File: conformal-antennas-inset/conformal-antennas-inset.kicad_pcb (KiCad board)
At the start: 2 copper layers, 1 part, among them J1 Conn_Coaxial

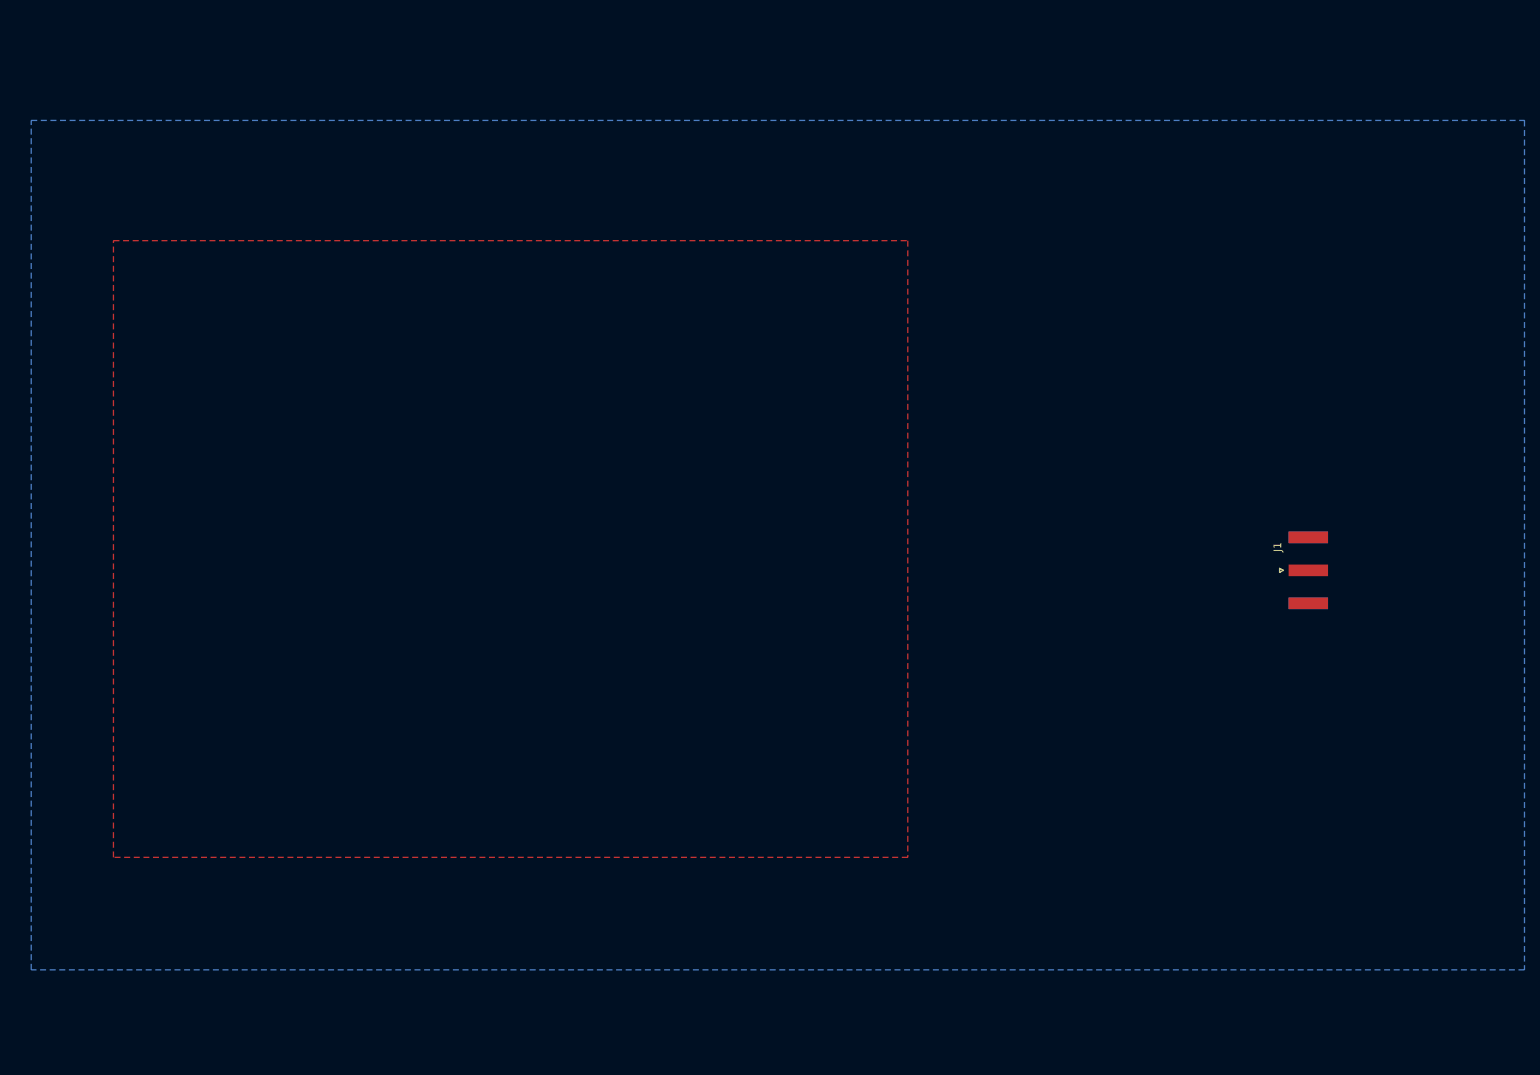
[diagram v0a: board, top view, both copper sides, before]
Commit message: added inset shape
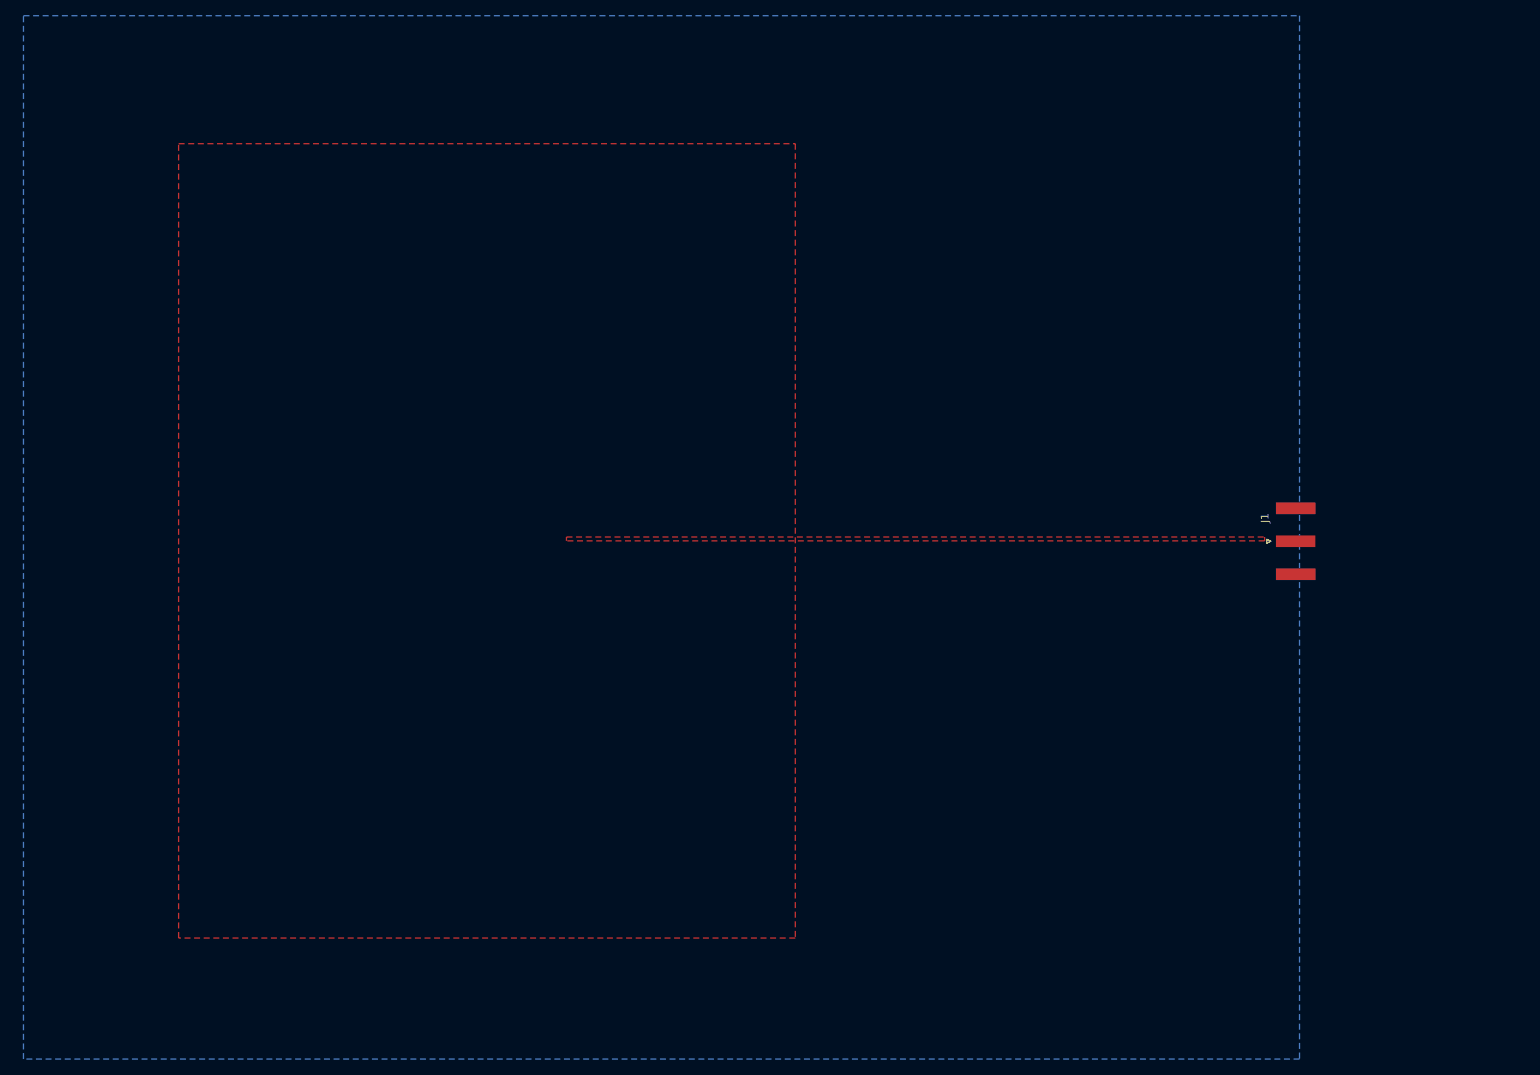
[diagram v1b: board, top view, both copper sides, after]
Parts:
- moved J1 4.09 mm to (213.5, 103.8)
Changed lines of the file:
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@@
 	(footprint "Connector_Coaxial:SMA_Amphenol_132289_EdgeMount"
 		(layer "F.Cu")
-		(at 215.1375 107.5)
+		(at 213.5 103.75)
 		(descr "https://www.amphenolrf.com/library/download/link/link_id/595984/parent/132289/")
 		(tags "SMA")
@@
 		(layer "F.Cu")
 		(hatch edge 0.5)
-		(connect_pads
+		(priority 1)
+		(connect_pads yes
 			(clearance 0.5)
 		)
@@
 		(polygon
 			(pts
-				(xy 61.1 65) (xy 163.5 65) (xy 163.5 144.5) (xy 61.1 144.5)
+				(xy 119.5 103.2) (xy 209.5 103.2) (xy 209.5 103.7) (xy 119.5 103.7)
+			)
+		)
+	)
+	(zone
+		(net 2)
+		(net_name "/Signal")
+		(layer "F.Cu")
+		(hatch edge 0.5)
+		(connect_pads yes
+			(clearance 0.5)
+		)
+		(min_thickness 0.25)
+		(filled_areas_thickness no)
+		(fill yes
+			(thermal_gap 0.5)
+			(thermal_bridge_width 0.5)
+		)
+		(polygon
+			(pts
+				(xy 69.5 52.5) (xy 149 52.5) (xy 149 154.9) (xy 69.5 154.9)
+			)
+		)
+	)
+	(zone
+		(net 0)
+		(net_name "")
+		(layer "F.Cu")
+		(hatch edge 0.1)
+		(connect_pads yes
+			(clearance 0)
+		)
+		(min_thickness 0.25)
+		(filled_areas_thickness no)
+		(keepout
+			(tracks not_allowed)
+			(vias not_allowed)
+			(pads not_allowed)
+			(copperpour not_allowed)
+			(footprints allowed)
+		)
+		(placement
+			(enabled no)
+			(sheetname "/")
+		)
+		(fill
+			(thermal_gap 0.5)
+			(thermal_bridge_width 0.5)
+		)
+		(polygon
+			(pts
+				(xy 119.5 103.7) (xy 149 103.7) (xy 149 104.2) (xy 119.5 104.2)
+			)
+		)
+	)
+	(zone
+		(net 0)
+		(net_name "")
+		(layer "F.Cu")
+		(hatch edge 0.1)
+		(connect_pads yes
+			(clearance 0)
+		)
+		(min_thickness 0.25)
+		(filled_areas_thickness no)
+		(keepout
+			(tracks not_allowed)
+			(vias not_allowed)
+			(pads not_allowed)
+			(copperpour not_allowed)
+			(footprints allowed)
+		)
+		(placement
+			(enabled no)
+			(sheetname "/")
+		)
+		(fill
+			(thermal_gap 0.5)
+			(thermal_bridge_width 0.5)
+		)
+		(polygon
+			(pts
+				(xy 119.5 102.7) (xy 149 102.7) (xy 149 103.2) (xy 119.5 103.2)
 			)
 		)
@@
 		(layer "B.Cu")
 		(hatch edge 0.5)
-		(connect_pads
+		(connect_pads yes
 			(clearance 0.5)
 		)
@@
 		(polygon
 			(pts
-				(xy 50.5 49.5) (xy 243 49.5) (xy 243 159) (xy 50.5 159)
-			)
-		)
+				(xy 49.5 36) (xy 214 36) (xy 214 170.5) (xy 49.5 170.5)
+			)
+		)

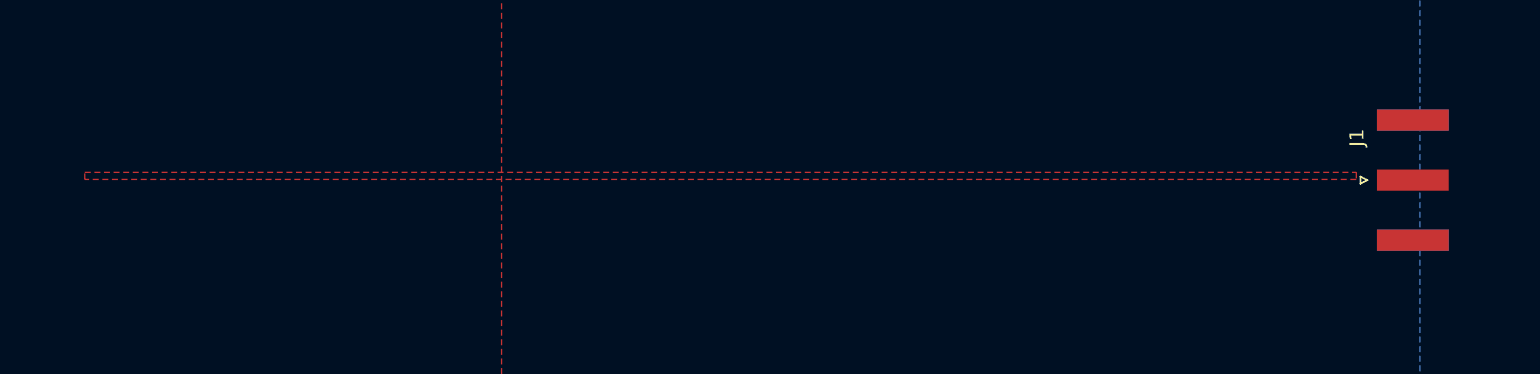
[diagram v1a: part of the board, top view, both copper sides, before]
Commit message: Inset
Added ground patch, vias and trace
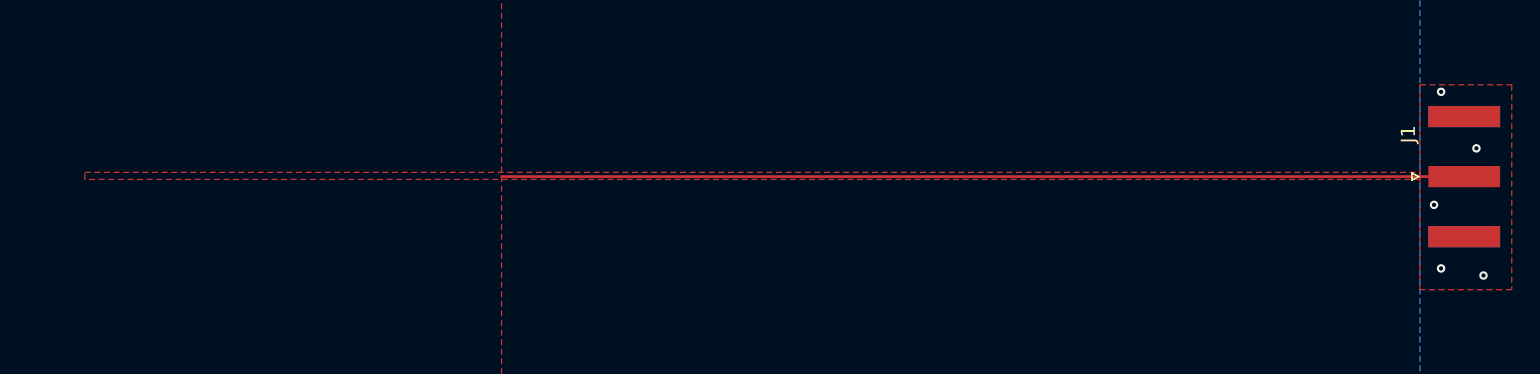
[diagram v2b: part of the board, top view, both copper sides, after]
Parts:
- moved J1 3.65 mm to (217.1, 103.5)
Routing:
- net /Signal: track 0.00 -> 68.1 mm
- net GND: vias 0 -> 5
- added copper zone on F.Cu, net GND
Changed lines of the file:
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@@
 	(footprint "Connector_Coaxial:SMA_Amphenol_132289_EdgeMount"
 		(layer "F.Cu")
-		(at 213.5 103.75)
+		(at 217.1375 103.5)
 		(descr "https://www.amphenolrf.com/library/download/link/link_id/595984/parent/132289/")
 		(tags "SMA")
@@
 		)
 	)
+	(via
+		(at 215.5 110)
+		(size 0.6)
+		(drill 0.3)
+		(layers "F.Cu" "B.Cu")
+		(free yes)
+		(net 1)
+	)
+	(via
+		(at 218.5 110.5)
+		(size 0.6)
+		(drill 0.3)
+		(layers "F.Cu" "B.Cu")
+		(free yes)
+		(net 1)
+	)
+	(via
+		(at 218 101.5)
+		(size 0.6)
+		(drill 0.3)
+		(layers "F.Cu" "B.Cu")
+		(free yes)
+		(net 1)
+	)
+	(via
+		(at 215.5 97.5)
+		(size 0.6)
+		(drill 0.3)
+		(layers "F.Cu" "B.Cu")
+		(free yes)
+		(net 1)
+	)
+	(via
+		(at 215 105.5)
+		(size 0.6)
+		(drill 0.3)
+		(layers "F.Cu" "B.Cu")
+		(free yes)
+		(net 1)
+	)
+	(segment
+		(start 217.1375 103.5)
+		(end 149 103.5)
+		(width 0.2)
+		(layer "F.Cu")
+		(net 2)
+	)
 	(zone
 		(net 2)
@@
 		(polygon
 			(pts
-				(xy 119.5 103.2) (xy 209.5 103.2) (xy 209.5 103.7) (xy 119.5 103.7)
+				(xy 119.5 103.2) (xy 214 103.2) (xy 214 103.7) (xy 119.5 103.7)
 			)
 		)
@@
 			)
 		)
+	)
+	(zone
+		(net 1)
+		(net_name "GND")
+		(layer "F.Cu")
+		(hatch edge 0.5)
+		(priority 2)
+		(connect_pads
+			(clearance 0.5)
+		)
+		(min_thickness 0.25)
+		(filled_areas_thickness no)
+		(fill yes
+			(thermal_gap 0.5)
+			(thermal_bridge_width 0.5)
+		)
+		(polygon
+			(pts
+				(xy 214 97) (xy 220.5 97) (xy 220.5 111.5) (xy 214 111.5)
+			)
+		)

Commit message: inset: fixed edge cuts maybe??
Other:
- board outline added: 172.5 x 134.5 mm
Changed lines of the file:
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@@
 		)
+	)
+	(gr_line
+		(start 48.5 170.5)
+		(end 48.5 36)
+		(stroke
+			(width 0.05)
+			(type default)
+		)
+		(layer "Edge.Cuts")
+	)
+	(gr_line
+		(start 49.5 36)
+		(end 221 36)
+		(stroke
+			(width 0.05)
+			(type default)
+		)
+		(layer "Edge.Cuts")
+	)
+	(gr_line
+		(start 221 170.5)
+		(end 48.5 170.5)
+		(stroke
+			(width 0.05)
+			(type default)
+		)
+		(layer "Edge.Cuts")
+	)
+	(gr_line
+		(start 221 36)
+		(end 221 170.5)
+		(stroke
+			(width 0.05)
+			(type default)
+		)
+		(layer "Edge.Cuts")
 	)
 	(via
